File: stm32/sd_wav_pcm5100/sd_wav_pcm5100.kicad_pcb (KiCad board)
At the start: 2 copper layers, 41 parts, among them J1 BTN_1-4, J2 BTN_5-7, J3 BTN_8-11, P1 ST-LINK, P2 SPK_OUTL, P3 SPK_OUTR, U1 STM32F410RBT6, U2 PCM5100, U3 PAM8403, U4 MX-503398-1892

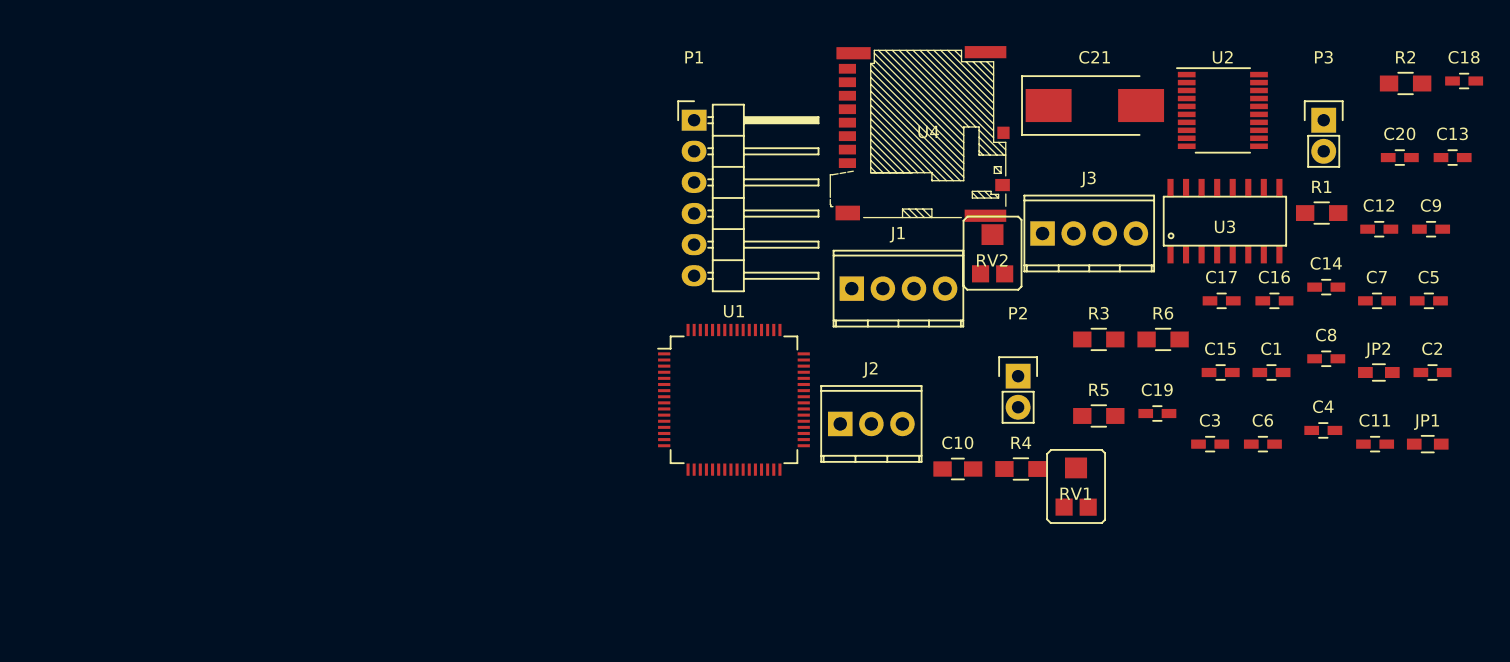
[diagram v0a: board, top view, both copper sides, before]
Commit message: [sd_wav_pcm5100] pcb routing 1st pass
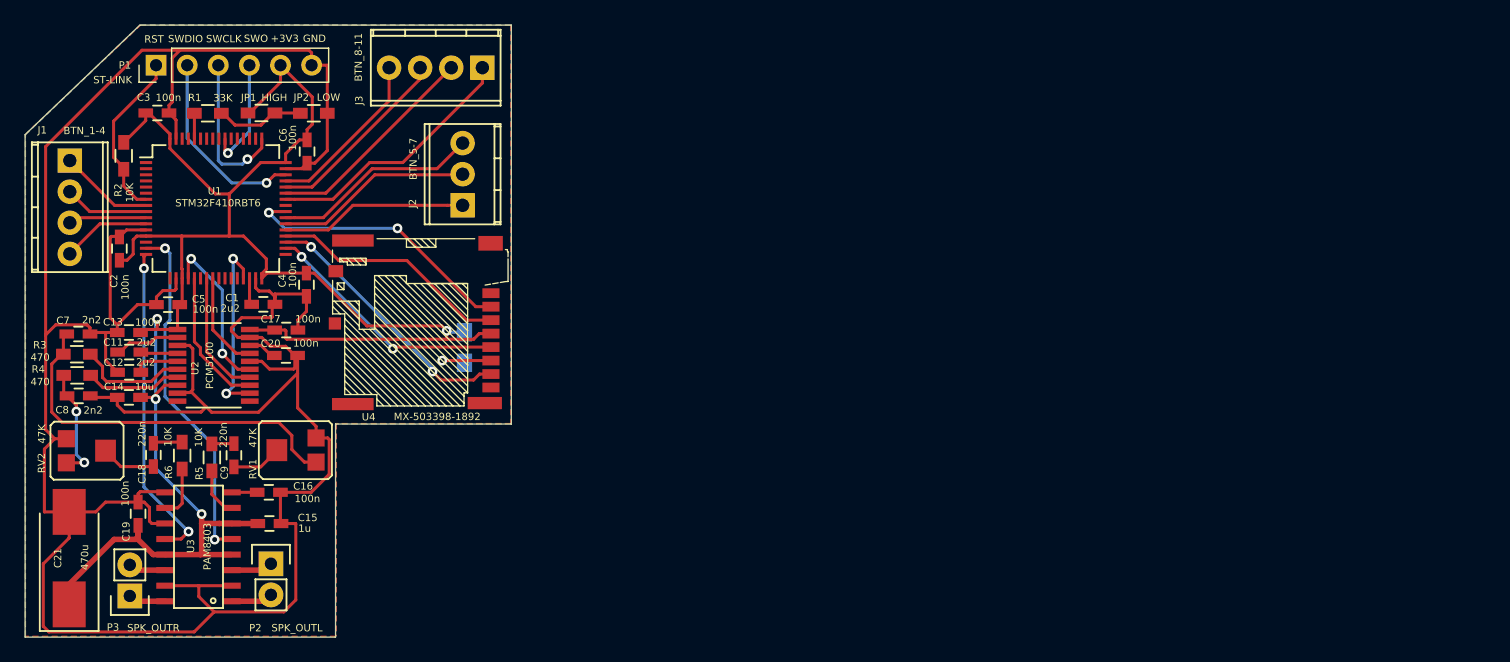
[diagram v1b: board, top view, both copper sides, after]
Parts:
- C10: moved to B.Cu
- P1: footprint Pin_Headers:Pin_Header_Angled_1x06 -> Pin_Headers:Pin_Header_Straight_1x06_Pitch2.54mm
- R1, R2, R3, R4, R5, R6: footprint Resistors_SMD:R_0805_HandSoldering -> Resistors_SMD:R_0603_HandSoldering
- moved C18 111.3 mm to (69.6, 103.5), turned to 90 degrees
- moved C13 109.0 mm to (67.6, 93.5), turned to 180 degrees
- moved C2 107.7 mm to (66.8, 86.7), turned to 90 degrees
- moved C7 106.1 mm to (63.5, 93.7), turned to 180 degrees
- moved P3 104.9 mm to (67.7, 115.0), turned to 180 degrees
- moved R2 104.8 mm to (67.2, 79.1), turned to 90 degrees
- moved C12 103.0 mm to (67.6, 98.8)
- moved C5 103.0 mm to (70.8, 91.2), turned to 180 degrees
- moved C11 102.0 mm to (67.6, 95.1), turned to 180 degrees
- moved C8 101.9 mm to (63.5, 98.7), turned to 180 degrees
- moved C9 99.5 mm to (76.2, 103.5), turned to 270 degrees
- moved JP1 99.0 mm to (78.4, 75.6), turned to 180 degrees
- moved C14 98.0 mm to (67.6, 96.8), turned to 180 degrees
- moved C20 92.4 mm to (80.4, 95.4)
- moved C21 91.5 mm to (62.7, 112.0), turned to 90 degrees
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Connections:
- U1 pad 1: Net-(U1-Pad1) -> (no net)
- U1 pad 14: Net-(U1-Pad14) -> (no net)
- U1 pad 17: Net-(U1-Pad17) -> (no net)
- U1 pad 2: Net-(U1-Pad2) -> (no net)
- U1 pad 22: Net-(U1-Pad22) -> (no net)
- U1 pad 25: Net-(U1-Pad25) -> (no net)
- U1 pad 26: Net-(U1-Pad26) -> (no net)
- U1 pad 27: Net-(U1-Pad27) -> (no net)
- U1 pad 28: Net-(U1-Pad28) -> (no net)
- U1 pad 3: Net-(U1-Pad3) -> (no net)
- U1 pad 33: Net-(U1-Pad33) -> (no net)
- U1 pad 4: Net-(U1-Pad4) -> (no net)
- U1 pad 41: Net-(U1-Pad41) -> (no net)
- U1 pad 5: Net-(U1-Pad5) -> (no net)
- U1 pad 50: Net-(U1-Pad50) -> (no net)
- U1 pad 51: Net-(U1-Pad51) -> (no net)
- U1 pad 52: Net-(U1-Pad52) -> (no net)
- U1 pad 53: Net-(U1-Pad53) -> (no net)
- U1 pad 54: Net-(U1-Pad54) -> (no net)
- U1 pad 56: Net-(U1-Pad56) -> (no net)
- U1 pad 57: Net-(U1-Pad57) -> (no net)
- U1 pad 58: Net-(U1-Pad58) -> (no net)
- U1 pad 59: Net-(U1-Pad59) -> (no net)
- U1 pad 6: Net-(U1-Pad6) -> (no net)
- U1 pad 61: Net-(U1-Pad61) -> (no net)
- U1 pad 62: Net-(U1-Pad62) -> (no net)
- U2 pad 10: Net-(U2-Pad10) -> (no net)
- U2 pad 11: Net-(U2-Pad11) -> (no net)
- U4 pad 1: Net-(U4-Pad1) -> (no net)
- U4 pad 10: Net-(U4-Pad10) -> (no net)
- U4 pad 8: Net-(U4-Pad8) -> (no net)
- U4 pad 9: Net-(U4-Pad9) -> (no net)
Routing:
- net GND: track 0.00 -> 247.2 mm, vias 0 -> 1
- net +3V3: track 0.00 -> 154.1 mm, vias 0 -> 4
- net /PCM5100_OUTL: track 0.00 -> 31.0 mm
- net /PAM8403_MUTE: track 0.00 -> 28.7 mm, vias 0 -> 2
- net /PAM8403_STANDBY: track 0.00 -> 26.3 mm, vias 0 -> 2
- net /SD_CS: track 0.00 -> 22.7 mm, vias 0 -> 2
- net /SD_DO: track 0.00 -> 21.8 mm, vias 0 -> 2
- net /BTN8: track 0.00 -> 21.2 mm
- net /SD_SCLK: track 0.00 -> 20.3 mm, vias 0 -> 2
- net /SD_DI: track 0.00 -> 19.6 mm
- net /BTN9: track 0.00 -> 17.8 mm
- net /BTN7: track 0.00 -> 17.0 mm
- net /BTN6: track 0.00 -> 16.1 mm
- net /SWDIO: track 0.00 -> 15.8 mm, vias 0 -> 1
- net /BTN10: track 0.00 -> 15.6 mm
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- added copper zone on B.Cu, net GND
- added copper zone on F.Cu, net GND
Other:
- board outline added: 39.7 x 50 mm
- net class Default: clearance 0.2 -> 0.25
- rule trace_clearance: 0.2 -> 0.25
- board text added: "+3V3"
- board text added: "GND"
- board text added: "RST"
- board text added: "SWCLK"
- board text added: "SWDIO"
- board text added: "SWO"

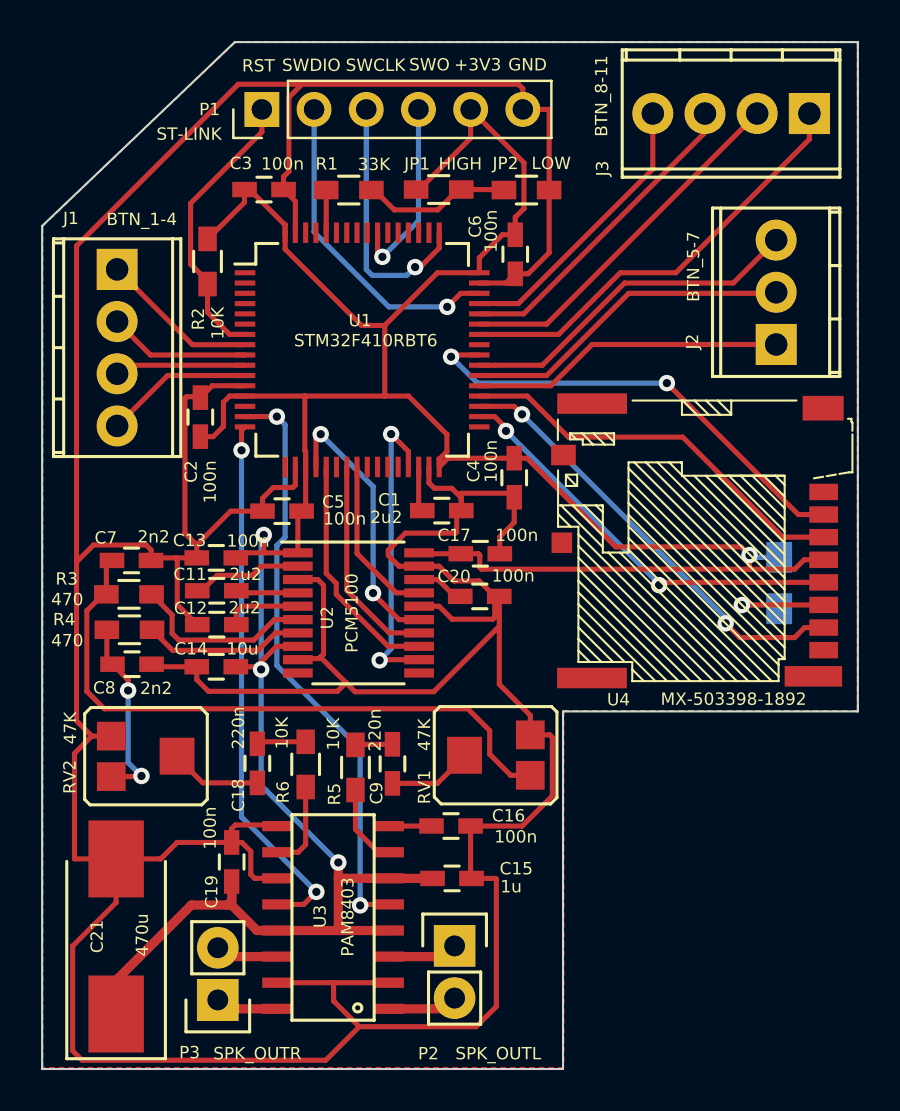
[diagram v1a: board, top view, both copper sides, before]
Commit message: [sd_wav_pcm5100] pcb routing 2nd pass
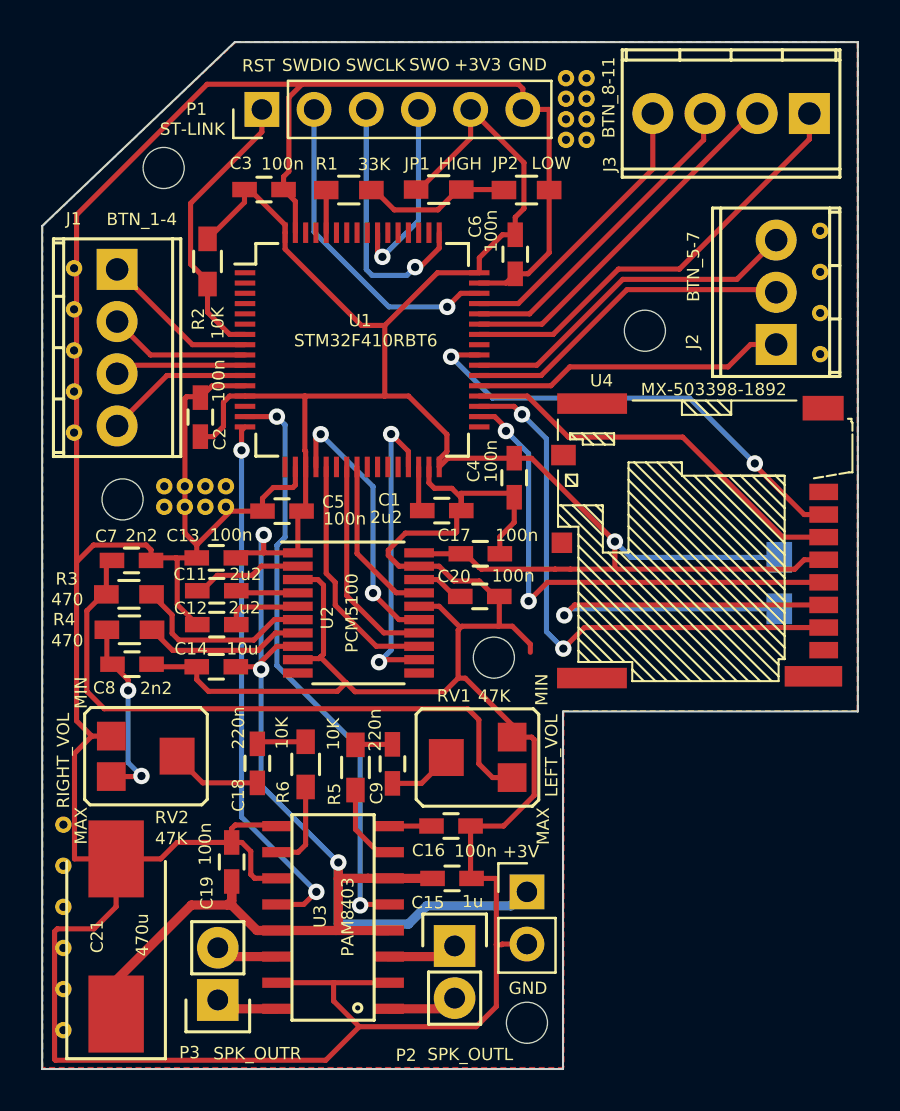
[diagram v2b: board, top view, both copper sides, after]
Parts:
- added P4: Supply, Pin_Headers:Pin_Header_Straight_1x02_Pitch2.54mm, F.Cu at (82.7, 109.8)
- added REF**: 1pin, myfootprints:1pin, F.Cu at (97.0, 83.6)
- added REF**: 1pin, myfootprints:1pin, F.Cu at (60.2, 116.5)
- added REF**: 1pin, myfootprints:1pin, F.Cu at (60.2, 114.5)
- added REF**: 1pin, myfootprints:1pin, F.Cu at (60.2, 112.5)
- added REF**: 1pin, myfootprints:1pin, F.Cu at (60.2, 110.5)
- added REF**: 1pin, myfootprints:1pin, F.Cu at (60.2, 108.5)
- added REF**: 1pin, myfootprints:1pin, F.Cu at (60.2, 106.5)
- added REF**: 1pin, myfootprints:1pin, F.Cu at (66.1, 91.0)
- added REF**: 1pin, myfootprints:1pin, F.Cu at (67.1, 90.0)
- added REF**: 1pin, myfootprints:1pin, F.Cu at (66.1, 90.0)
- added REF**: 1pin, myfootprints:1pin, F.Cu at (65.1, 90.0)
- added REF**: 1pin, myfootprints:1pin, F.Cu at (97.0, 81.6)
- added REF**: 1pin, myfootprints:1pin, F.Cu at (65.1, 91.0)
- added REF**: 1pin, myfootprints:1pin, F.Cu at (68.1, 90.0)
- added REF**: 1pin, myfootprints:1pin, F.Cu at (67.1, 91.0)
- added REF**: 1pin, myfootprints:1pin, F.Cu at (68.1, 91.0)
- added REF**: 1pin, myfootprints:1pin, F.Cu at (85.6, 73.2)
- added REF**: 1pin, myfootprints:1pin, F.Cu at (84.6, 73.2)
- added REF**: 1pin, myfootprints:1pin, F.Cu at (85.6, 72.2)
- added REF**: 1pin, myfootprints:1pin, F.Cu at (84.6, 72.2)
- added REF**: 1pin, myfootprints:1pin, F.Cu at (85.6, 71.2)
- added REF**: 1pin, myfootprints:1pin, F.Cu at (84.6, 71.2)
- added REF**: 1pin, myfootprints:1pin, F.Cu at (97.0, 79.6)
- added REF**: 1pin, myfootprints:1pin, F.Cu at (85.6, 70.2)
- added REF**: 1pin, myfootprints:1pin, F.Cu at (84.6, 70.2)
- added REF**: hole_2mm, myfootprints:hole_2mm, F.Cu at (81.1, 98.4)
- added REF**: hole_2mm, myfootprints:hole_2mm, F.Cu at (65.0, 74.5)
- added REF**: hole_2mm, myfootprints:hole_2mm, F.Cu at (88.5, 82.5)
- added REF**: hole_2mm, myfootprints:hole_2mm, F.Cu at (63.0, 90.7)
- added REF**: hole_2mm, myfootprints:hole_2mm, F.Cu at (82.7, 116.2)
- added REF**: 1pin, myfootprints:1pin, F.Cu at (97.0, 77.6)
- added REF**: 1pin, myfootprints:1pin, F.Cu at (60.7, 81.4)
- added REF**: 1pin, myfootprints:1pin, F.Cu at (60.7, 83.4)
- added REF**: 1pin, myfootprints:1pin, F.Cu at (60.7, 79.4)
- added REF**: 1pin, myfootprints:1pin, F.Cu at (60.7, 87.4)
- added REF**: 1pin, myfootprints:1pin, F.Cu at (60.7, 85.4)
- added REF***: OSHW-Logo_7.5x8mm_SilkScreen, Symbols:OSHW-Logo_7.5x8mm_SilkScreen, B.Cu at (69.1, 81.0)
- moved RV1 0.89 mm to (80.4, 103.3)
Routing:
- net GND: track 247.2 -> 268.2 mm
- net +3V3: track 154.1 -> 167.2 mm
- net /SD_DO: track 21.8 -> 27.6 mm
- net /SD_SCLK: track 20.3 -> 25.2 mm
- net Net-(C9-Pad2): track 4.10 -> 3.17 mm
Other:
- board text added: "+3V"
- board text added: "LEFT_VOL"
- board text added: "MAX"
- board text added: "MIN"
- board text added: "RIGHT_VOL"
- board text added: "WAV Sound Module"
